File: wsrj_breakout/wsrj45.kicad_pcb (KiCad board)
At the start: 2 copper layers, 48.3 x 95.9 mm, 33 parts, among them J1 OCTO_WS, J10 Conn_01x03, J11 Conn_01x03, J12 Conn_01x03, J13 Conn_01x01, J14 Conn_01x01, J15 Conn_01x01, J16 Conn_01x01, J17 pwr, J2 OCTO_WS, J3 DC_IN, J4 DC_IN, J5 DATA_1, J6 DATA_2, J7 DATA_3, J8 DATA_4, J9 Conn_01x03

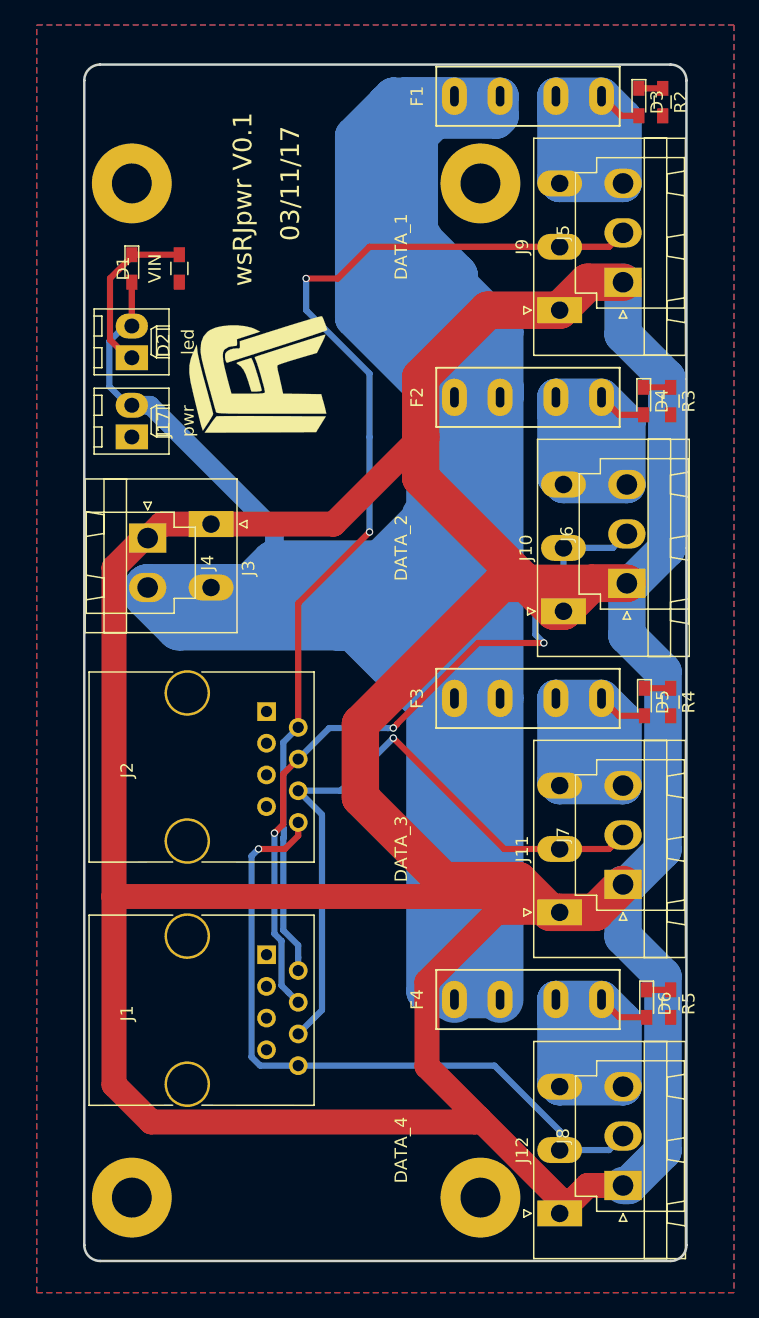
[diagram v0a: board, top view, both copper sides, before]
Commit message: v02 of power distribution
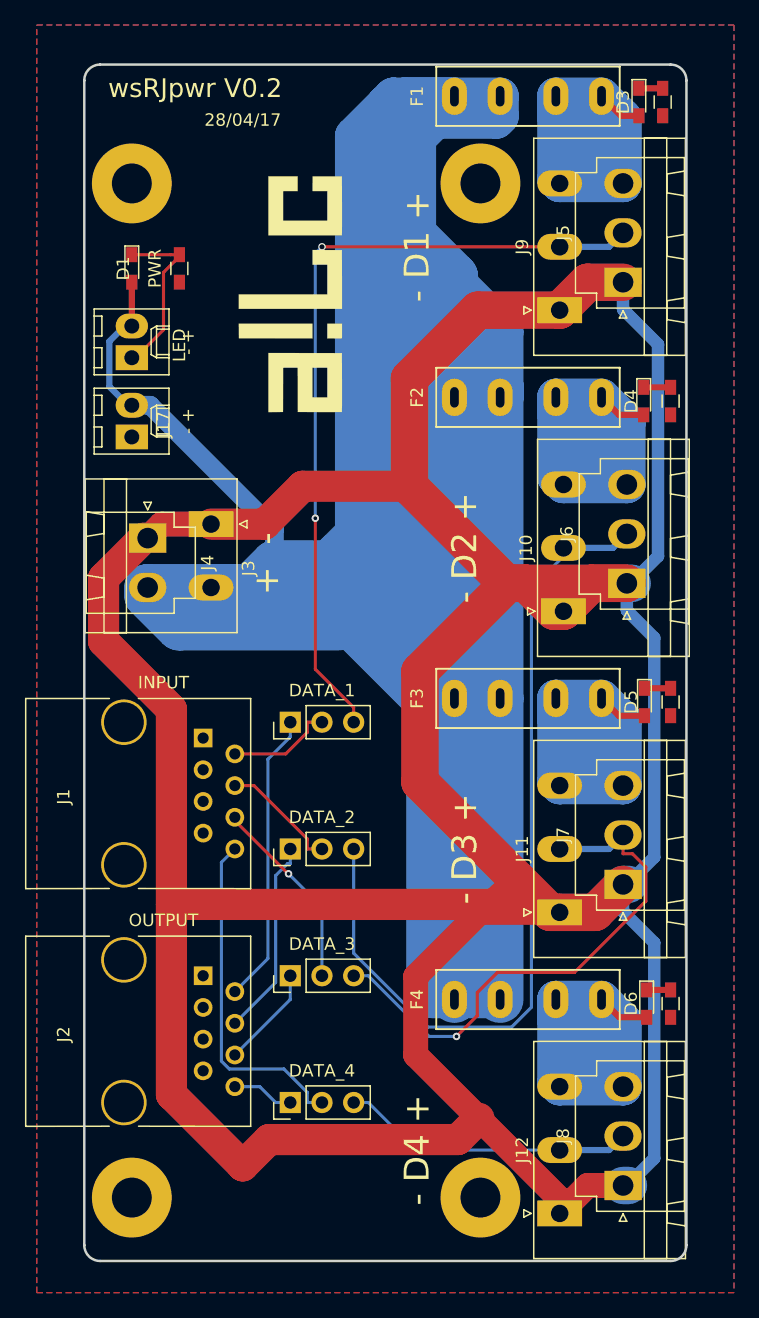
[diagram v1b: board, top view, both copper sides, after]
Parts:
- removed the G*** at (91.4, 81.3)
- added G***: LOGO, alc_kicad_library:alc_logo_21_5mm, F.Cu at (94.0, 74.9)
- added J18: DATA_4, Socket_Strips:Socket_Strip_Straight_1x03_Pitch2.54mm, F.Cu at (94.0, 139.7)
- added J19: DATA_3, Socket_Strips:Socket_Strip_Straight_1x03_Pitch2.54mm, F.Cu at (94.0, 129.5)
- added J20: DATA_2, Socket_Strips:Socket_Strip_Straight_1x03_Pitch2.54mm, F.Cu at (94.0, 119.4)
- added J21: DATA_1, Socket_Strips:Socket_Strip_Straight_1x03_Pitch2.54mm, F.Cu at (94.0, 109.2)
- D1: value VIN -> PWR
- J1: value OCTO_WS -> INPUT; footprint Connectors:RJ45_8 -> robocut_footprint:RJ45_8_54602-908LF
- J17: value pwr -> - +
- J2: value OCTO_WS -> OUTPUT; footprint Connectors:RJ45_8 -> robocut_footprint:RJ45_8_54602-908LF
- LED: renamed from D2; value led -> - +
- moved J2 21.8 mm to (87.0, 129.5)
- moved J1 18.1 mm to (87.0, 110.5)
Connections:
- J1 pad 2: /DATA_1 -> Net-(J1-Pad2)
- J1 pad 4: /DATA_2 -> Net-(J1-Pad4)
- J1 pad 6: /DATA_3 -> Net-(J1-Pad6)
- J1 pad 8: /DATA_4 -> Net-(J1-Pad8)
- J2 pad 2: /DATA_1 -> Net-(J2-Pad2)
- J2 pad 4: /DATA_2 -> Net-(J2-Pad4)
- J2 pad 6: /DATA_3 -> Net-(J19-Pad1)
- J2 pad 8: /DATA_4 -> Net-(J18-Pad1)
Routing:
- net VCC: track 393.8 -> 451.6 mm
- net /DATA_4: track 55.8 -> 23.6 mm, vias 1 -> 0
- net Net-(J1-Pad8): track 0.00 -> 27.4 mm
- net /DATA_1: track 87.9 -> 64.2 mm
- net Net-(J2-Pad2): track 0.00 -> 23.4 mm
- net Net-(J2-Pad4): track 0.00 -> 15.9 mm
- net Net-(J1-Pad6): track 0.00 -> 15.6 mm, vias 0 -> 1
- net /DATA_2: track 59.0 -> 69.4 mm, vias 3 -> 0
- net GND: track 364.0 -> 353.7 mm
- net /DATA_3: track 53.0 -> 43.0 mm
- net Net-(J1-Pad4): track 0.00 -> 9.56 mm
- net Net-(J1-Pad2): track 0.00 -> 8.51 mm
- net Net-(J19-Pad1): track 0.00 -> 8.19 mm
- net Net-(J18-Pad1): track 0.00 -> 4.97 mm
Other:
- board text added: "+ -"
- board text added: "- D1 +"
- board text added: "- D2 +"
- board text added: "- D3 +"
- board text added: "- D4 +"
- board text added: "28/04/17"
- board text added: "wsRJpwr V0.2"
- board text removed: "03/11/17"
- board text removed: "wsRJpwr V0.1"
